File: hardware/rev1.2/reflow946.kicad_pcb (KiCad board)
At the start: 2 copper layers, 104 x 60 mm, 63 parts, among them J1 VH-2A, J2 VH-3A2, J3 VH-3A2, J4 XH-A2, J5 HDR-M-2.54_2x3, J6 TFT_1.47, J7 PROBE_BRK, J8 EXT_TC, Q1 BTA16-600BRG, Q2 MMBT3906, Q3 MMBT3906, Q4 MMBT3906, SW1 SW_Push, SW2 SW_Push, SW3 SW_Push, U1 MOC3041M, U2 ESP32-WROOM-32U, U3 MAX31855KASA, U4 AMS1117-3.3, U6 MAX31855KASA

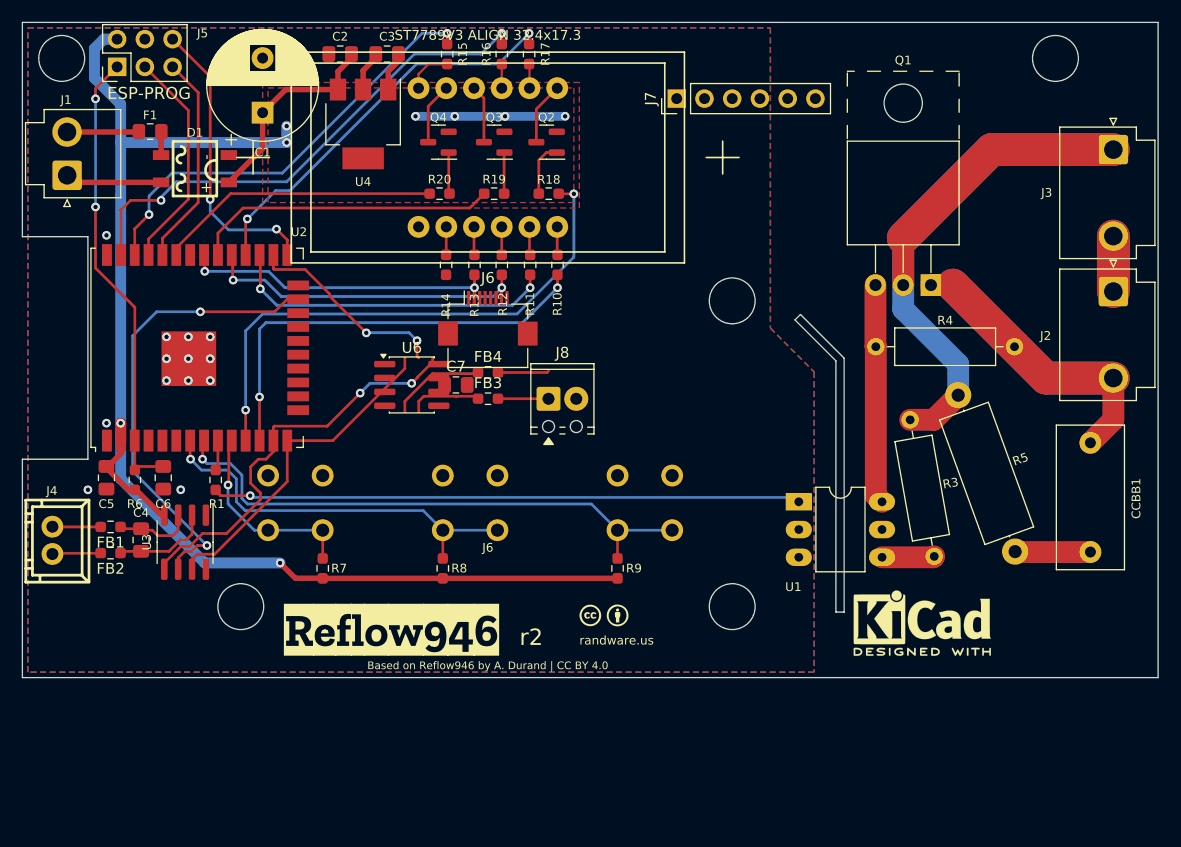
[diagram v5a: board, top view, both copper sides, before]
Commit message: rev2: add J9 2.54mm breakout header mirroring J6 FPC signals
- J9 PinHeader_1x08 @ bottom strip (142.6,124.3), same tail order:
  1=dp(BL) 2=f(CS) 3=d(DC) 4=g(RES) 5=c(SDA) 6=d2(SCL) 7=+3V3 8=GND
- Schematic: J9 symbol + label cluster cloned beside J6's
- Enables bench bring-up via pogo/dupont to standard display breakouts
  while the FH12 rehearses the v2 FPC mounting path
- Caveat: one display attached at a time (shared SPI bus)
- DRC: zero electrical violations; 16 unrouted pads remain (J6/J9 escapes)
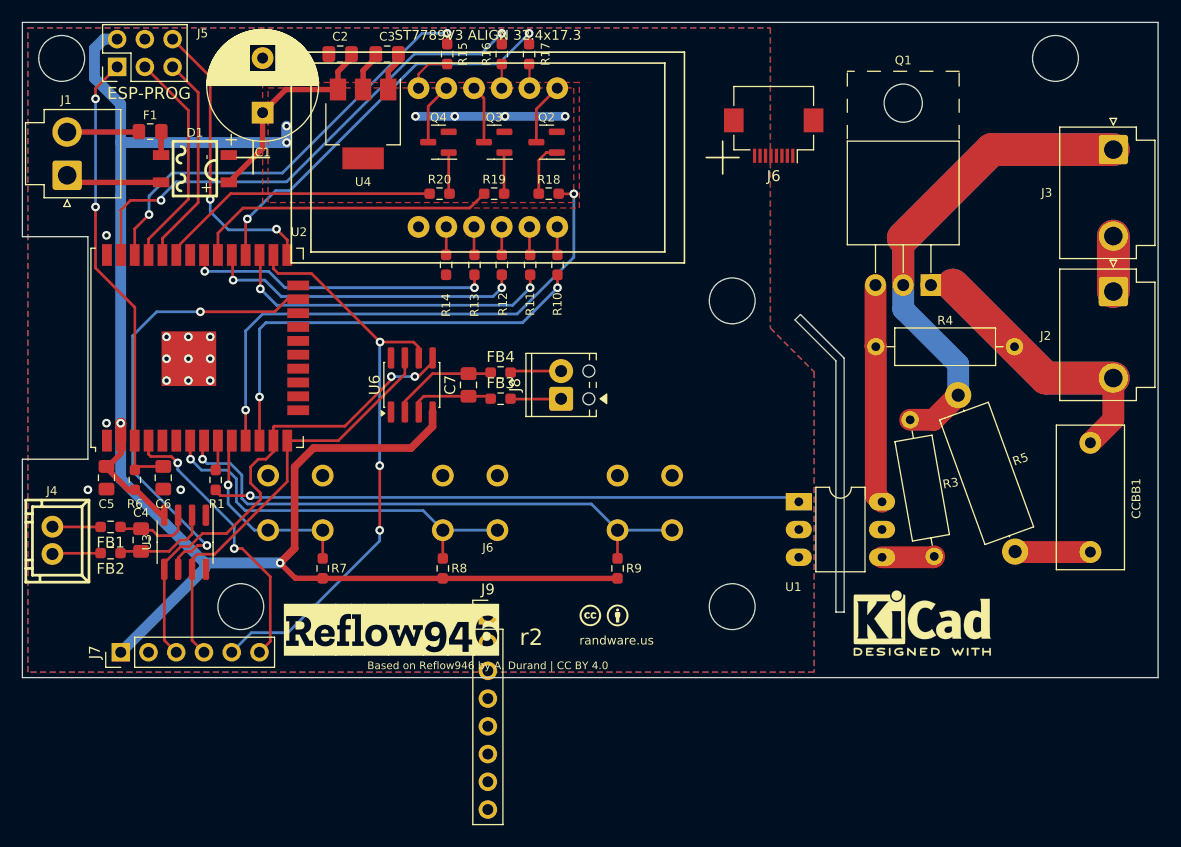
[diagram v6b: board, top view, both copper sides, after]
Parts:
- added J9: TFT_BRK, PinHeader_1x08_P2.54mm_Vertical, F.Cu at (142.6, 124.3)
- moved J7 71.8 mm to (109.0, 127.7)
- moved J6 31.1 mm to (168.8, 80.4), turned to 180 degrees
- moved C7 1.15 mm to (140.9, 103.2), turned to 90 degrees
- moved FB3 1.15 mm to (143.8, 104.5)
- moved FB4 1.15 mm to (143.8, 102.1)
- moved J8 1.15 mm to (149.3, 104.5), turned to 90 degrees
- turned U6 to 90 degrees
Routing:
- net +3.3V: track 139.0 -> 175.2 mm
- net /CS_EXT: track 18.9 -> 54.5 mm, vias 2 -> 3
- net /TC_ADC: track 0.00 -> 25.9 mm, vias 0 -> 2
- net /MISO: track 31.0 -> 39.4 mm
- net /CLK: track 37.7 -> 45.9 mm
- net Net-(U6-T-): track 8.77 -> 10.1 mm
- net Net-(U6-T+): track 6.69 -> 7.84 mm

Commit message: manufacturing: JLC export bundle + final DRC pass
- Gerbers (7 layers), Excellon drill + map, JLC-format CPL (34 SMD,
  Y-flipped, THT stripped, DNP excluded), grouped JLC BOM (29 lines)
- DRC rule severities: silk/text/mismatch classes -> warning
- DRC final: 0 unconnected, 0 shorts/clearance/hole violations;
  remaining = silk cosmetics + baseline lib-version drift only
- BOM gap report: LCSC part numbers needed for new parts (J6/J7/J9,
  U6, C7, FB1-FB4, R6-R20 passives)
- README: interface description updated (FH12 + J9, shared-bus caveat)
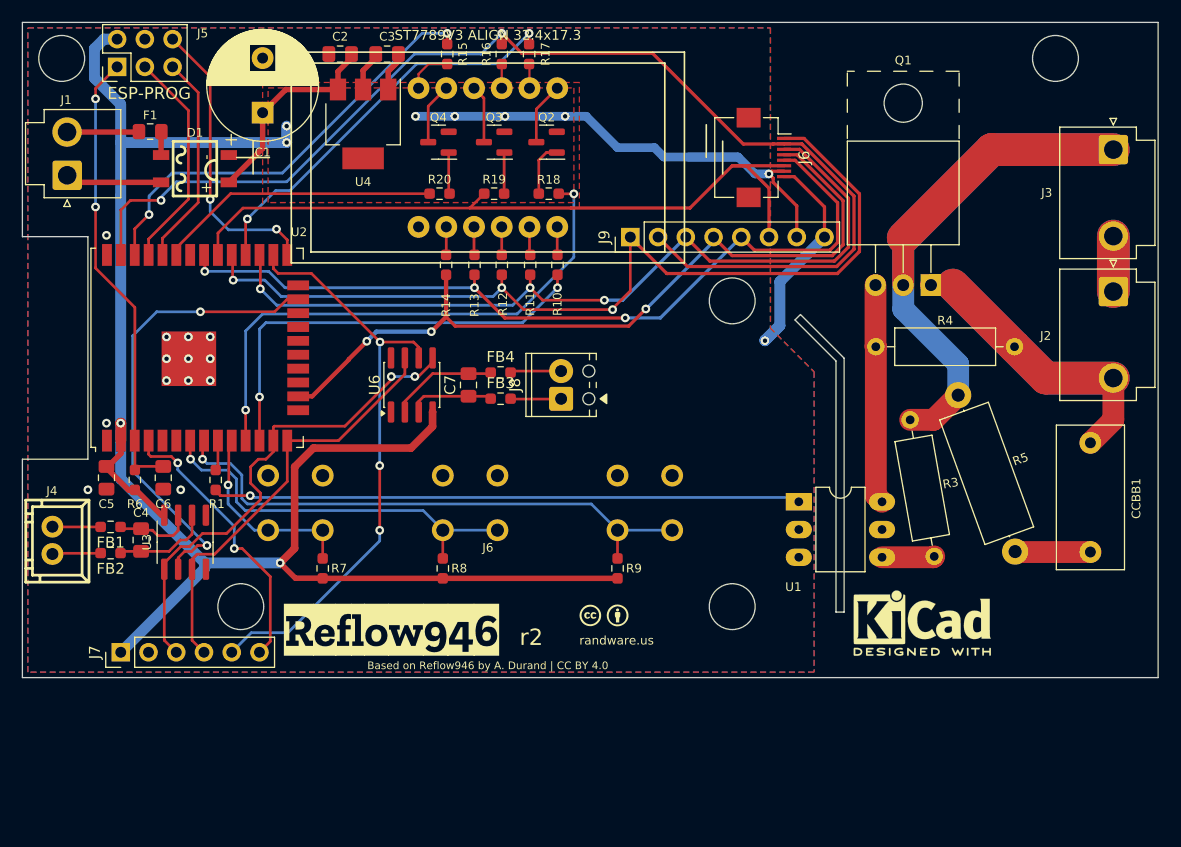
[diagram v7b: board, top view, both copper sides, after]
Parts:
- J6: footprint Hirose_FH12-8S-0.5SH_1x08-1MP_P0.50mm_Horizontal -> Connector_FFC-FPC:Hirose_FH12-8S-0.5SH_1x08-1MP_P0.50mm_Horizontal
- J9: value TFT_BRK -> TFT_1.47; footprint PinHeader_1x08_P2.54mm_Vertical -> Connector_PinHeader_2.54mm:PinHeader_1x08_P2.54mm_Vertical
- moved J9 37.0 mm to (155.7, 89.7), turned to 90 degrees
- moved J6 2.20 mm to (167.9, 82.4), turned to -90 degrees
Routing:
- net /g: track 0.00 -> 73.1 mm, vias 0 -> 3
- net /f: track 46.9 -> 109.9 mm
- net /dp: track 29.1 -> 84.8 mm, vias 2 -> 3
- net /c: track 28.0 -> 76.4 mm, vias 2 -> 3
- net /d: track 30.3 -> 76.0 mm, vias 2 -> 3
- net /d2: track 27.9 -> 67.0 mm
- net +3.3V: track 175.2 -> 209.3 mm, vias 8 -> 9
- net GND: track 3.64 -> 25.0 mm, vias 13 -> 14

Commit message: Fabricate Randware v2.0 revision
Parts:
- removed the REF** at (182.4, 125.0)
- moved J2 4.20 mm to (195.7, 94.7)
- moved J3 4.19 mm to (195.7, 81.7)
- moved kibuzzard-632CED8E 3.75 mm to (137.6, 125.6)
- moved R4 1.67 mm to (176.5, 99.7)
- moved CCBB1 1.24 mm to (196.6, 118.5)
- moved R5 0.44 mm to (190.5, 118.5)
- moved J7 0.19 mm to (109.0, 127.9)
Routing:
- net Net-(J2-Pin_2): track 47.3 -> 38.3 mm
- net Net-(J3-Pin_1): track 71.3 -> 62.8 mm
- net Net-(J2-Pin_1): track 10.2 -> 5.08 mm
- net Net-(Q1-G): track 20.1 -> 21.5 mm
- net Net-(CCBB1-Pad1): track 6.91 -> 5.67 mm
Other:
- board size 104 x 60 mm -> 100 x 60 mm
- board text removed: "J6"
